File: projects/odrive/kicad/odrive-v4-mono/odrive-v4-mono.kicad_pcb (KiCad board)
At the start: 4 copper layers, 140 x 112 mm, 325 parts, among them J1 PC 16/2-ST, J10 ENC_M1_JST-GH, J11 ENC_SPI_JST-GH, J12 GPIO_2x4, J13 BRAKE_EXT, J2 M0 A/B/C, J4 FTSH-105-01-L-DV-K, J5 FAN 12V 150mA MAX, J6 USB4105-GF-A, J7 JST-GH-4 CAN, J8 JST-GH-4 CAN, J9 ENC_M0_JST-GH, Q1 NVMFS5C628NL | BSC027N10NS5, Q10 NVMFS5C628NL, Q11 NVMFS5C628NL, Q12 NVMFS5C628NL, Q13 NVMFS5C628NL, Q14 NVMFS5C628NL, Q15 NVMFS5C628NL, Q16 NVMFS5C628NL, Q17 NVMFS5C628NL, Q18 NVMFS5C628NL, Q19 NVMFS5C628NL, Q20 NVMFS5C628NL, Q21 NVMFS5C628NL, Q50 NVMFS5C628NL/BSC027N10NS5, Q51 NVMFS5C628NL/BSC027N10NS5, SW1 CAN_TERM, U10 TLV9062, U11 TMUX1204, U12 TLV7031, U13 TLV431, U14 74LVC1G04, U15 74LVC1G08, U16 TPD4E05U06, U2 STM32F405RGT6, U20 LM5164DDA, U21 LMR51430, U22 TLV75533PDBV, U23 TPS7A2033DBV, U25 74LVC1G06, U26 TLV7031DBV, U27 74LVC1G08, U28 TPS3840DL30, U3 DRV8353RS, U30 TPS2553DBV, U31 TPS2553DBV, U32 TPS2553DBV, U33 USBLC6-2SC6, U34 TCAN1042HGV, U35 SN74LVC2G17, U36 SN74LVC2G17, U37 SN74LVC2G17, U38 TPD4E05U06, U39 TPD4E05U06, U40 SN74LVC1G125, U41 TPD4E05U06, U42 TPD1E10B06, U50 UCC27517A, U51 INA181A2, U52 TLV7031, U53 74LVC1G74, U54 74LVC1G32, U55 74LVC1G08, Y1 8MHz

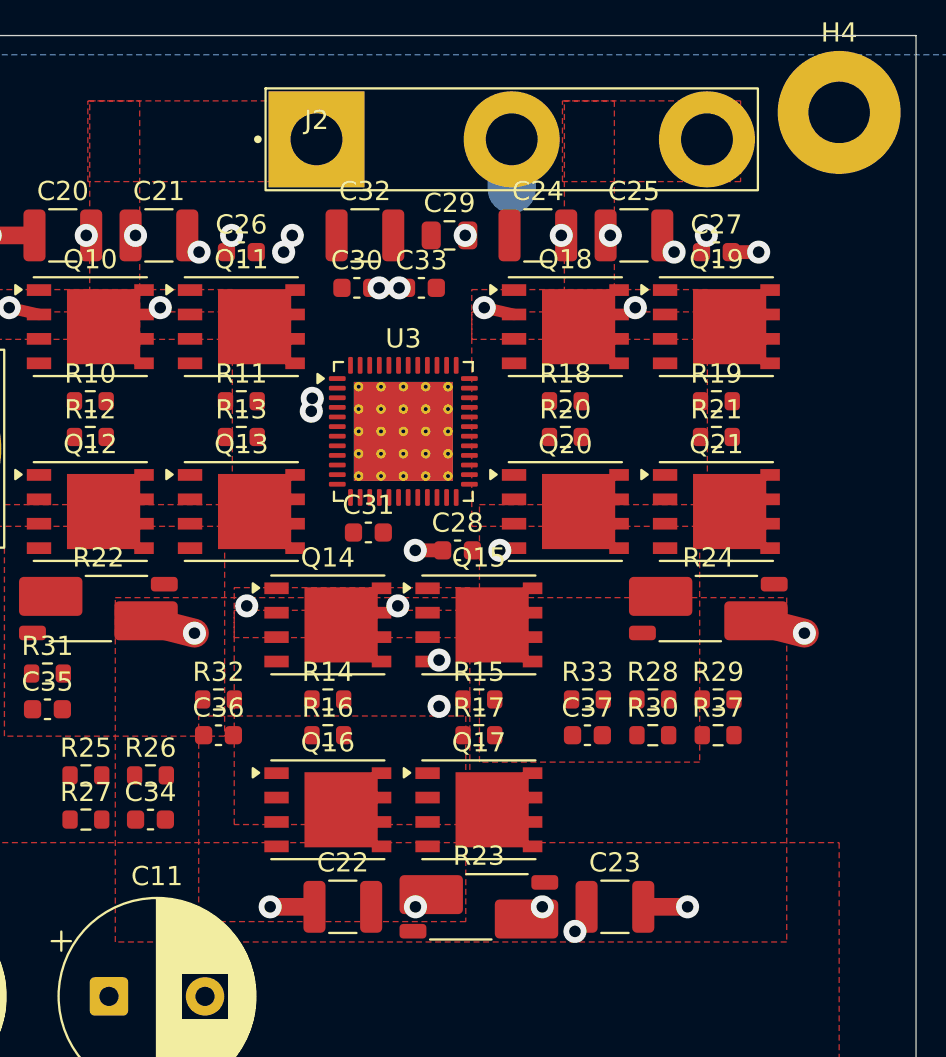
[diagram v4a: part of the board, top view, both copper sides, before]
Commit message: Phase 0: power routing DRC-clean - zero errors
From 55 to 0 in one systematic round, each error class killed at its
root instead of case by case:

- Power pours now connect SOLID instead of thermal-relief (16 zones):
  at 40A the starved-spoke errors were the tool telling us thermal
  reliefs do not belong on power pads. All 14 starved_thermal gone.
- Same-footprint geometry is the library's business, not the board
  rule's: a .kicad_dru pair scoped to A.Reference == B.Reference (0.1mm
  clearance, 0.15mm hole) clears the MSOP mux and USB shell-peg
  violations without touching the board-wide 0.2mm.
- NT1/NT2 net-ties and JP1/JP2 solder jumpers declared as what they
  are: net_tie_pad_groups + allow_soldermask_bridges attributes. Their
  copper deliberately bridges; DRC now knows.
- Three DCBUS stitch vias deleted (each drain pad keeps its sibling
  via + the In2 plane), one PGND and the M0_B corridor via slid to
  spots verified against pads AND vias - the earlier free-spot search
  only checked pads, which is exactly how those vias landed 1.4mm from
  neighbours.
- The B-phase B.Cu corridor rebuilt three times until the pre-check
  passed against all 48 vias: the final path drops from the cluster,
  runs the y=91.5 lane, and climbs x=169.5 through the one 4.01mm gap
  in the C-drain via row - which fits a 2.0mm track with 1.85mm margins
  but not a 2.5mm one. Every segment now verified in code BEFORE
  writing, then confirmed by DRC after refill.

kicad-cli pcb drc: 0 violations. 499 unconnected items remain - that
is the signal-routing backlog for Phase 2 (freerouting), per
docs/routing-strategy.md. Next: power evaluators, rule areas over the
gate loops, then lock everything.
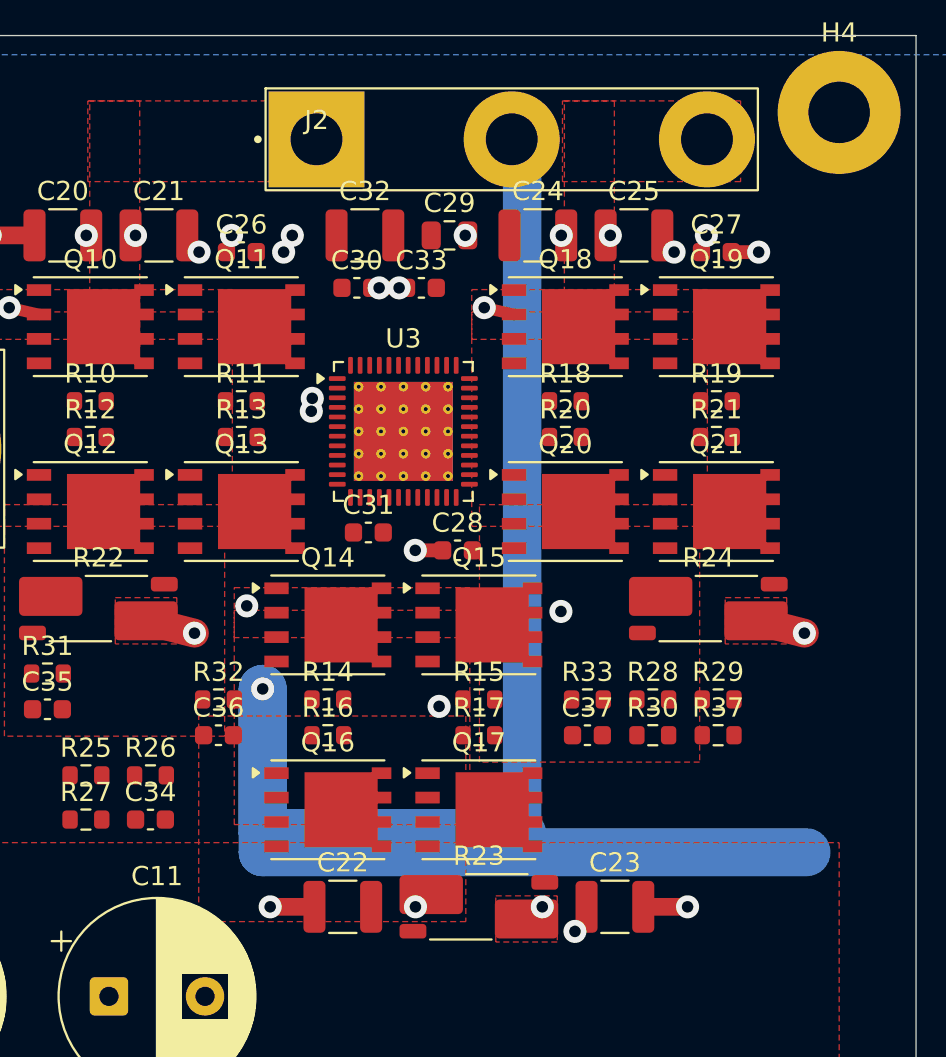
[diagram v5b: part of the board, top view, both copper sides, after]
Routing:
- net /MotorCell M0/M0_B: track 2.60 -> 94.0 mm
- net DCBUS: vias 26 -> 23
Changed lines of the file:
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@@
 			)
 		)
+		(net_tie_pad_groups "1,2")
 		(duplicate_pad_numbers_are_jumpers no)
 		(fp_poly
@@
 			)
 		)
+		(net_tie_pad_groups "1,2")
 		(duplicate_pad_numbers_are_jumpers no)
 		(fp_poly
@@
 			)
 		)
+		(attr smd allow_soldermask_bridges)
+		(net_tie_pad_groups "1,2")
 		(duplicate_pad_numbers_are_jumpers no)
 		(fp_poly
@@
 			)
 		)
+		(attr smd allow_soldermask_bridges)
+		(net_tie_pad_groups "1,2")
 		(duplicate_pad_numbers_are_jumpers no)
 		(fp_poly
@@
 	)
 	(via
-		(at 163.03 79.68)
-		(size 1.2)
-		(drill 0.6)
-		(layers "F.Cu" "B.Cu")
-		(net "DCBUS")
-	)
-	(via
 		(at 167.53 64.16)
 		(size 1.2)
@@
 	)
 	(via
-		(at 150.67 64.16)
-		(size 1.2)
-		(drill 0.6)
-		(layers "F.Cu" "B.Cu")
-		(net "DCBUS")
-	)
-	(via
-		(at 175.39 64.16)
-		(size 1.2)
-		(drill 0.6)
-		(layers "F.Cu" "B.Cu")
-		(net "DCBUS")
-	)
-	(via
 		(at 155.17 79.68)
 		(size 1.2)
@@
 	)
 	(via
-		(at 168.34 76.79)
+		(at 171.52 79.97)
 		(size 1.2)
 		(drill 0.6)
@@
 	)
 	(via
-		(at 165.18 82.5)
+		(at 156 84)
 		(size 1.2)
 		(drill 0.6)
@@
 	)
 	(segment
-		(start 168.96 58)
-		(end 168.96 55.4)
+		(start 156 84)
+		(end 156 92.5)
+		(width 2.5)
+		(layer "B.Cu")
+		(net "/MotorCell M0/M0_B")
+	)
+	(segment
+		(start 156 92.5)
+		(end 184.3 92.5)
+		(width 2.5)
+		(layer "B.Cu")
+		(net "/MotorCell M0/M0_B")
+	)
+	(segment
+		(start 156 84)
+		(end 156 91.5)
 		(width 2.5)
 		(layer "B.Cu")
 		(net "/MotorCell M0/M0_B")
 	)
+	(segment
+		(start 156 91.5)
+		(end 169.5 91.5)
+		(width 2.5)
+		(layer "B.Cu")
+		(net "/MotorCell M0/M0_B")
+	)
+	(segment
+		(start 169.5 91.5)
+		(end 169.5 57.5)
+		(width 2)
+		(layer "B.Cu")
+		(net "/MotorCell M0/M0_B")
+	)
+	(segment
+		(start 169.5 57.5)
+		(end 168.96 55.4)
+		(width 2)
+		(layer "B.Cu")
+		(net "/MotorCell M0/M0_B")
+	)
 	(via
 		(at 163.95 95.34)
@@
 	)
 	(zone
+		(net "PGND")
+		(layer "F.Cu")
+		(name "PGND R23")
+		(hatch edge 0.508)
+		(priority 5)
+		(connect_pads yes
+			(clearance 0.3)
+		)
+		(min_thickness 0.25)
+		(fill yes
+			(thermal_gap 0.5)
+			(thermal_bridge_width 0.5)
+			(island_removal_mode 0)
+		)
+		(polygon
+			(pts
+				(xy 168.13 94.77) (xy 171.33 94.77) (xy 171.33 97.17) (xy 168.13 97.17)
+			)
+		)
+	)
+	(zone
+		(net "PGND")
+		(layer "F.Cu")
+		(name "PGND R22")
+		(hatch edge 0.508)
+		(priority 5)
+		(connect_pads yes
+			(clearance 0.3)
+		)
+		(min_thickness 0.25)
+		(fill yes
+			(thermal_gap 0.5)
+			(thermal_bridge_width 0.5)
+			(island_removal_mode 0)
+		)
+		(polygon
+			(pts
+				(xy 148.33 79.25) (xy 151.53 79.25) (xy 151.53 81.66) (xy 148.33 81.66)
+			)
+		)
+	)
+	(zone
+		(net "PGND")
+		(layer "F.Cu")
+		(name "PGND R24")
+		(hatch edge 0.508)
+		(priority 5)
+		(connect_pads yes
+			(clearance 0.3)
+		)
+		(min_thickness 0.25)
+		(fill yes
+			(thermal_gap 0.5)
+			(thermal_bridge_width 0.5)
+			(island_removal_mode 0)
+		)
+		(polygon
+			(pts
+				(xy 180.07 79.25) (xy 183.27 79.25) (xy 183.27 81.66) (xy 180.07 81.66)
+			)
+		)
+	)
+	(zone
 		(net "/MotorCell M0/M0_SRC_A")
 		(layer "F.Cu")
@@
 		(hatch edge 0.508)
 		(priority 5)
-		(connect_pads
+		(connect_pads yes
 			(clearance 0.3)
 		)
@@
 		(hatch edge 0.508)
 		(priority 4)
-		(connect_pads
+		(connect_pads yes
 			(clearance 0.3)
 		)
@@
 		(hatch edge 0.508)
 		(priority 2)
-		(connect_pads
+		(connect_pads yes
 			(clearance 0.5)
 		)
@@
 		(hatch edge 0.508)
 		(priority 6)
-		(connect_pads
+		(connect_pads yes
 			(clearance 0.3)
 		)
@@
 		(hatch edge 0.508)
 		(priority 5)
-		(connect_pads
+		(connect_pads yes
 			(clearance 0.3)
 		)
@@
 		(hatch edge 0.508)
 		(priority 3)
-		(connect_pads
+		(connect_pads yes
 			(clearance 0.3)
 		)
@@
 		(hatch edge 0.508)
 		(priority 6)
-		(connect_pads
+		(connect_pads yes
 			(clearance 0.3)
 		)
@@
 		(hatch edge 0.508)
 		(priority 5)
-		(connect_pads
+		(connect_pads yes
 			(clearance 0.3)
 		)
@@
 		(hatch edge 0.508)
 		(priority 5)
-		(connect_pads
+		(connect_pads yes
 			(clearance 0.3)
 		)
@@
 		(hatch edge 0.508)
 		(priority 4)
-		(connect_pads
+		(connect_pads yes
 			(clearance 0.3)
 		)
@@
 	)
 	(zone
-		(net "PGND")
-		(layer "F.Cu")
-		(name "PGND shunt band")
-		(hatch edge 0.508)
-		(priority 5)
-		(connect_pads
-			(clearance 0.3)
-		)
-		(min_thickness 0.25)
-		(fill yes
-			(thermal_gap 0.5)
-			(thermal_bridge_width 0.5)
-			(island_removal_mode 0)
-		)
-		(polygon
-			(pts
-				(xy 148.33 79.25) (xy 183.27 79.25) (xy 183.27 97.17) (xy 148.33 97.17)
-			)
-		)
-	)
-	(zone
 		(net "DCBUS")
 		(layer "F.Cu")
@@
 		(hatch edge 0.508)
 		(priority 6)
-		(connect_pads
+		(connect_pads yes
 			(clearance 0.3)
 		)
@@
 		(hatch edge 0.508)
 		(priority 1)
-		(connect_pads
+		(connect_pads yes
 			(clearance 0.5)
 		)
@@
 		(hatch edge 0.508)
 		(priority 5)
-		(connect_pads
+		(connect_pads yes
 			(clearance 0.3)
 		)
@@
 		(hatch edge 0.508)
 		(priority 5)
-		(connect_pads
+		(connect_pads yes
 			(clearance 0.3)
 		)
@@
 		(hatch edge 0.508)
 		(priority 3)
-		(connect_pads
+		(connect_pads yes
 			(clearance 0.3)
 		)
